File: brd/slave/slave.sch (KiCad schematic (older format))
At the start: 23 parts, among them IC1 ATMEGA328P-A, P1 CONN_3X2, P2 CONN_8, P3 CONN_2, P4 CONN_6, P5 CONN_1, Q1 BC847, U1 LM78L05ACZ, X1 16MHz

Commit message: layout rework & gerber generation for slave pcb
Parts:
- P1: value CONN_3X2 -> AVRISP
- P2: value CONN_8 -> IO; footprint Pin_Headers:Pin_Header_Angled_1x08 -> Pin_Headers:Pin_Header_Straight_1x08
- P3: value CONN_2 -> PIEZO; footprint Pin_Headers:Pin_Header_Angled_1x02 -> Pin_Headers:Pin_Header_Straight_1x02
- P4: value CONN_6 -> DEBUG; footprint Pin_Headers:Pin_Header_Angled_1x06 -> Pin_Headers:Pin_Header_Straight_1x06
- renumbered IC1 to U2
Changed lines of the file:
@@
 LIBS:valves
 LIBS:slave-cache
-EELAYER 24 0
+EELAYER 25 0
 EELAYER END
 $Descr A4 11693 8268
@@
 Sheet 1 1
 Title "Open wound"
-Date "29 jul 2014"
+Date "sáb 06 dic 2014"
 Rev "rc2"
 Comp "Synusia"
 Comment1 "Under MIT License"
 Comment2 ""
-Comment3 ""
+Comment3 "Designed by kwendenarmo"
 Comment4 "Slave layout"
 $EndDescr
 $Comp
-L ATMEGA328P-A IC1
+L ATMEGA328P-A U2
 U 1 1 53D78762
 P 5900 4250
-F 0 "IC1" H 5150 5500 40  0000 L BNN
+F 0 "U2" H 5150 5500 40  0000 L BNN
 F 1 "ATMEGA328P-A" H 6300 2850 40  0000 L BNN
 F 2 "SMD_Packages:TQFP32" H 5900 4250 30  0001 C CIN
@@
 P 7950 2800
 F 0 "P1" H 7950 3050 50  0000 C CNN
-F 1 "CONN_3X2" V 7950 2850 40  0000 C CNN
+F 1 "AVRISP" V 7950 2850 40  0000 C CNN
 F 2 "Pin_Headers:Pin_Header_Straight_2x03" H 7950 2800 60  0001 C CNN
 F 3 "" H 7950 2800 60  0000 C CNN
@@
 P 3350 3900
 F 0 "P2" V 3300 3900 60  0000 C CNN
-F 1 "CONN_8" V 3400 3900 60  0000 C CNN
-F 2 "Pin_Headers:Pin_Header_Angled_1x08" H 3350 3900 60  0001 C CNN
+F 1 "IO" V 3400 3900 60  0000 C CNN
+F 2 "Pin_Headers:Pin_Header_Straight_1x08" H 3350 3900 60  0001 C CNN
 F 3 "" H 3350 3900 60  0000 C CNN
 	1    3350 3900
@@
 P 8850 4900
 F 0 "P4" V 8800 4900 60  0000 C CNN
-F 1 "CONN_6" V 8900 4900 60  0000 C CNN
-F 2 "Pin_Headers:Pin_Header_Angled_1x06" H 8850 4900 60  0001 C CNN
+F 1 "DEBUG" V 8900 4900 60  0000 C CNN
+F 2 "Pin_Headers:Pin_Header_Straight_1x06" H 8850 4900 60  0001 C CNN
 F 3 "" H 8850 4900 60  0000 C CNN
 	1    8850 4900
@@
 P 3350 4700
 F 0 "P3" V 3300 4700 40  0000 C CNN
-F 1 "CONN_2" V 3400 4700 40  0000 C CNN
-F 2 "Pin_Headers:Pin_Header_Angled_1x02" H 3350 4700 60  0001 C CNN
+F 1 "PIEZO" V 3400 4700 40  0000 C CNN
+F 2 "Pin_Headers:Pin_Header_Straight_1x02" H 3350 4700 60  0001 C CNN
 F 3 "" H 3350 4700 60  0000 C CNN
 	1    3350 4700

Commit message: slave version rc3
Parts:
- removed C1, C2, C7: 100nF, Capacitors_SMD:c_0603, symbol C
- removed C3: 10uF, Capacitors_SMD:c_elec_5x5.3, symbol CAPAPOL
- removed C4: 1uF, Capacitors_SMD:c_elec_4x5.3, symbol CAPAPOL
- removed C5: 10nF, Capacitors_SMD:c_0603, symbol C
- removed C6, C8: 22pF, Capacitors_SMD:c_0603, symbol C
- removed C9: 100pF, Capacitors_SMD:c_0603, symbol C
- removed P1: AVRISP, Pin_Headers:Pin_Header_Straight_2x03, symbol CONN_3X2
- removed P2: IO, Pin_Headers:Pin_Header_Straight_1x08, symbol CONN_8
- removed P3: PIEZO, Pin_Headers:Pin_Header_Straight_1x02, symbol CONN_2
- removed P4: DEBUG, Pin_Headers:Pin_Header_Straight_1x06, symbol CONN_6
- removed P5: CONN_1, Wire_Pads:SolderWirePad_single_2mmDrill, symbol CONN_1
- removed X1: 16MHz, Crystals_Oscillators_SMD:Q_49U3HMS, symbol CRYSTAL
- added C1: 10uF, Capacitors_SMD:c_elec_5x5.3, symbol CP_Small
- added C2: 1uF, Capacitors_SMD:c_elec_4x5.3, symbol CP_Small
- added C3: 10nF, Capacitors_SMD:C_0603_HandSoldering, symbol C_Small
- added C4, C5, C7: 100nF, Capacitors_SMD:C_0603_HandSoldering, symbol C_Small
- added C6, C8: 22pF, Capacitors_SMD:C_0603_HandSoldering, symbol C_Small
- added C9: 100pF, Capacitors_SMD:C_0603_HandSoldering, symbol C_Small
- added P1: AVRISP, Pin_Headers:Pin_Header_Straight_2x03, symbol CONN_02X03
- added P2: IO, asrdi-conn:IL-Z-8PL-SMTYE, symbol CONN_01X08
- added P3: PIEZO, asrdi-conn:IL-Z-2PL-SMTYE, symbol CONN_01X02
- added P4: DEBUG, asrdi-conn:IL-Z-6PL-SMTYE, symbol CONN_01X06
- added P5: SENSE, Wire_Pads:SolderWirePad_single_2mmDrill, symbol CONN_01X01
- added X1: 16MHz, Crystals_Oscillators_SMD:Q_49U3HMS, symbol Crystal
- Q1: footprint Transistors_SMD:sot23 -> Housings_SOT-23_SOT-143_TSOT-6:SOT-23_Handsoldering
- R1, R2: footprint SMD_Packages:SM0603 -> Resistors_SMD:R_0603_HandSoldering
- R3, R4, R5: footprint SMD_Packages:SM0805 -> Resistors_SMD:R_0805_HandSoldering
- U2: footprint SMD_Packages:TQFP32 -> Housings_QFP:TQFP-32_7x7mm_Pitch0.8mm
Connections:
- net labels added: GNDA
- net labels removed: AGND
- wire segments 99 -> 102
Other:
- note added: "DEBUG\n1. +5V\n2. OUT (TTL)\n3. TX\n4. RX\n5. /RESET\n6. GND"
- note removed: "DEBUG\n1. +5V\n2. RX\n3. TX\n4. OUT (TTL)\n5. /RESET\n6. GND"
- moved on the sheet: U1

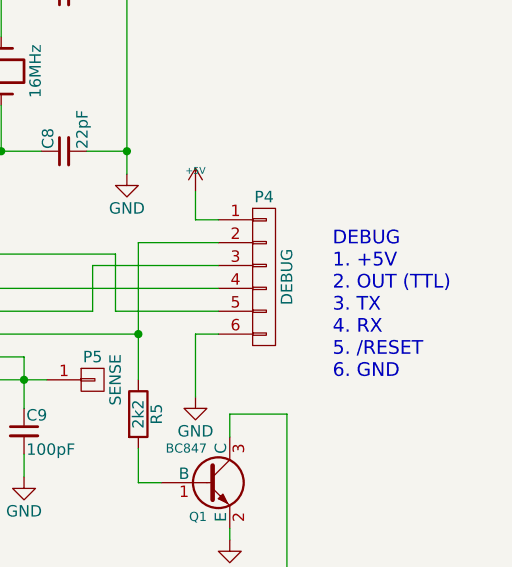
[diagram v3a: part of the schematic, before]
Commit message: versión slave 1.0.1 añadido BOM y referencias a esquemático
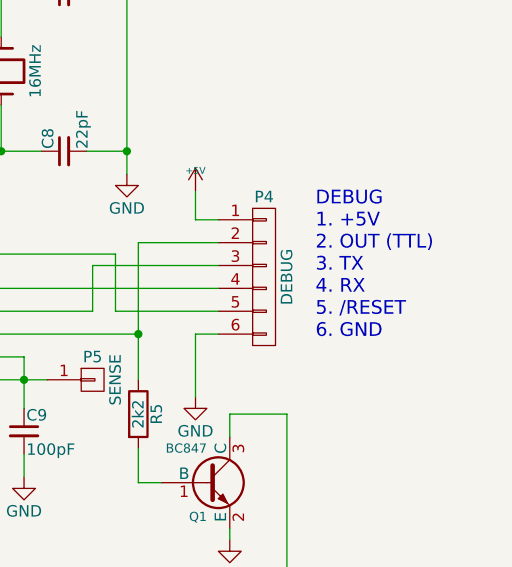
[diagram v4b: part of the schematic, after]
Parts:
- C1: Vendor (none) -> 140-VE100M1HTR0505
- C2: Vendor (none) -> 598-AVE105M50B12T-F
- C3: Vendor (none) -> 77-VJ0603Y103KXAAC
- C4, C5, C7: Vendor (none) -> 77-VJ0603Y104JXJPBC
- C6, C8: Vendor (none) -> 77-VJ0603A220JXACBC
- C9: Vendor (none) -> 77-VJ0603A101JXACBC
- P2: Vendor (none) -> 656-IL-Z-8PL-SMTYE
- P3: Vendor (none) -> 656-IL-Z-2PL-SMTYE
- P4: Vendor (none) -> 656-IL-Z-6PL-SMTYE
- Q1: Vendor (none) -> 583-BC847
- R1, R2: Vendor (none) -> 71-CRCW0603-10-E3
- R3: Vendor (none) -> 603-SR0805JR-0710KL
- R4: Vendor (none) -> 71-CRCW0805-1.0M-E3
- R5: Vendor (none) -> 660-RK73B2ATTD222J
- U1: Vendor (none) -> 821-TS78L05ACY
- U2: Vendor (none) -> 556-ATMEGA328P-AU
- X1: Vendor (none) -> 774-ATS16ASM-1
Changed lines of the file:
@@
 Sheet 1 1
 Title "Open wound"
-Date "2015-06-30"
-Rev "1.0.0"
+Date "2015-08-31"
+Rev "1.0.1"
 Comp "Synusia"
 Comment1 "Under GPLv3 License"
@@
 F 2 "Housings_QFP:TQFP-32_7x7mm_Pitch0.8mm" H 5900 4250 30  0001 C CIN
 F 3 "" H 5900 4250 60  0000 C CNN
+F 4 "556-ATMEGA328P-AU" H 5900 4250 60  0001 C CNN "Vendor"
 	1    5900 4250
 	1    0    0    -1
@@
 F 2 "Housings_SOT-89:SOT89-3_Housing_Handsoldering" H 3800 2250 30  0001 C CIN
 F 3 "" H 3800 2150 60  0000 C CNN
+F 4 "821-TS78L05ACY" H 3800 2150 60  0001 C CNN "Vendor"
 	1    3800 2150
 	1    0    0    -1
@@
 Text Notes 8250 2775 0    60   ~ 0
 AVR ISP
-Text Notes 9000 5150 0    60   ~ 0
+Text Notes 8925 4975 0    60   ~ 0
 DEBUG\n1. +5V\n2. OUT (TTL)\n3. TX\n4. RX\n5. /RESET\n6. GND
 Text Notes 2100 4300 0    60   ~ 0
@@
 F 2 "Housings_SOT-23_SOT-143_TSOT-6:SOT-23_Handsoldering" H 8350 5702 29  0001 C CNN
 F 3 "" H 8450 5600 60  0000 C CNN
+F 4 "583-BC847 " H 8450 5600 60  0001 C CNN "Vendor"
 	1    8450 5600
 	1    0    0    -1
@@
 F 2 "Capacitors_SMD:C_0603_HandSoldering" H 4450 2350 60  0001 C CNN
 F 3 "" H 4450 2350 60  0000 C CNN
+F 4 "77-VJ0603Y103KXAAC" H 4450 2350 60  0001 C CNN "Vendor"
 	1    4450 2350
 	1    0    0    -1
@@
 F 2 "Capacitors_SMD:c_elec_4x5.3" H 4250 2350 60  0001 C CNN
 F 3 "" H 4250 2350 60  0000 C CNN
+F 4 "598-AVE105M50B12T-F" H 4250 2350 60  0001 C CNN "Vendor"
 	1    4250 2350
 	1    0    0    -1
@@
 F 2 "Capacitors_SMD:c_elec_5x5.3" H 3350 2350 60  0001 C CNN
 F 3 "" H 3350 2350 60  0000 C CNN
+F 4 "140-VE100M1HTR0505 " H 3350 2350 60  0001 C CNN "Vendor"
 	1    3350 2350
 	1    0    0    -1
@@
 F 2 "Capacitors_SMD:C_0603_HandSoldering" H 5700 2350 60  0001 C CNN
 F 3 "" H 5700 2350 60  0000 C CNN
+F 4 "77-VJ0603Y104JXJPBC " H 5700 2350 60  0001 C CNN "Vendor"
 	1    5700 2350
 	1    0    0    -1
@@
 F 2 "Capacitors_SMD:C_0603_HandSoldering" H 6300 2350 60  0001 C CNN
 F 3 "" H 6300 2350 60  0000 C CNN
+F 4 "77-VJ0603Y104JXJPBC " H 6300 2350 60  0001 C CNN "Vendor"
 	1    6300 2350
 	1    0    0    -1
@@
 F 2 "Capacitors_SMD:C_0603_HandSoldering" H 7825 3450 60  0001 C CNN
 F 3 "" H 7825 3450 60  0000 C CNN
+F 4 "77-VJ0603A220JXACBC" H 7825 3450 60  0001 C CNN "Vendor"
 	1    7825 3450
 	0    -1   -1   0
@@
 F 2 "Capacitors_SMD:C_0603_HandSoldering" H 7825 4150 60  0001 C CNN
 F 3 "" H 7825 4150 60  0000 C CNN
+F 4 "77-VJ0603A220JXACBC" H 7825 4150 60  0001 C CNN "Vendor"
 	1    7825 4150
 	0    -1   -1   0
@@
 F 2 "Capacitors_SMD:C_0603_HandSoldering" H 7650 5375 60  0001 C CNN
 F 3 "" H 7650 5375 60  0000 C CNN
+F 4 "77-VJ0603A101JXACBC " H 7650 5375 60  0001 C CNN "Vendor"
 	1    7650 5375
 	1    0    0    -1
@@
 F 2 "Resistors_SMD:R_0603_HandSoldering" V 5930 2600 30  0001 C CNN
 F 3 "" H 6000 2600 30  0000 C CNN
+F 4 "71-CRCW0603-10-E3 " V 6000 2600 60  0001 C CNN "Vendor"
 	1    6000 2600
 	0    1    1    0
@@
 F 2 "Resistors_SMD:R_0603_HandSoldering" V 5930 2100 30  0001 C CNN
 F 3 "" H 6000 2100 30  0000 C CNN
+F 4 "71-CRCW0603-10-E3 " V 6000 2100 60  0001 C CNN "Vendor"
 	1    6000 2100
 	0    1    1    0
@@
 F 2 "Resistors_SMD:R_0805_HandSoldering" V 7655 3150 30  0001 C CNN
 F 3 "" H 7725 3150 30  0000 C CNN
+F 4 "603-SR0805JR-0710KL " V 7725 3150 60  0001 C CNN "Vendor"
 	1    7725 3150
 	0    1    1    0
@@
 F 2 "Resistors_SMD:R_0805_HandSoldering" V 7280 5150 30  0001 C CNN
 F 3 "" H 7350 5150 30  0000 C CNN
+F 4 "71-CRCW0805-1.0M-E3 " V 7350 5150 60  0001 C CNN "Vendor"
 	1    7350 5150
 	0    1    1    0
@@
 F 2 "Resistors_SMD:R_0805_HandSoldering" V 8080 5300 30  0001 C CNN
 F 3 "" H 8150 5300 30  0000 C CNN
+F 4 "660-RK73B2ATTD222J " V 8150 5300 60  0001 C CNN "Vendor"
 	1    8150 5300
 	1    0    0    -1
@@
 F 2 "Capacitors_SMD:C_0603_HandSoldering" H 4900 4000 60  0001 C CNN
 F 3 "" H 4900 4000 60  0000 C CNN
+F 4 "77-VJ0603Y104JXJPBC " H 4900 4000 60  0001 C CNN "Vendor"
 	1    4900 4000
 	1    0    0    -1
@@
 F 2 "Crystals_Oscillators_SMD:Q_49U3HMS" H 7550 3800 60  0001 C CNN
 F 3 "" H 7550 3800 60  0000 C CNN
+F 4 "774-ATS16ASM-1" H 7550 3800 60  0001 C CNN "Vendor"
 	1    7550 3800
 	0    -1   -1   0
@@
 F 2 "asrdi-conn:IL-Z-6PL-SMTYE" H 8700 4700 60  0001 C CNN
 F 3 "" H 8700 4700 60  0000 C CNN
+F 4 "656-IL-Z-6PL-SMTYE" H 8700 4700 60  0001 C CNN "Vendor"
 	1    8700 4700
 	1    0    0    -1
@@
 F 2 "asrdi-conn:IL-Z-2PL-SMTYE" H 3500 4650 60  0001 C CNN
 F 3 "" H 3500 4650 60  0000 C CNN
+F 4 "656-IL-Z-2PL-SMTYE " H 3500 4650 60  0001 C CNN "Vendor"
 	1    3500 4650
 	-1   0    0    -1
@@
 F 2 "asrdi-conn:IL-Z-8PL-SMTYE" H 3500 3900 60  0001 C CNN
 F 3 "" H 3500 3900 60  0000 C CNN
+F 4 "656-IL-Z-8PL-SMTYE" H 3500 3900 60  0001 C CNN "Vendor"
 	1    3500 3900
 	-1   0    0    -1
